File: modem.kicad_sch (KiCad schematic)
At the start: 14 parts, among them J1 A-1JB, J2 A-1JB, U1 BG95MxLA

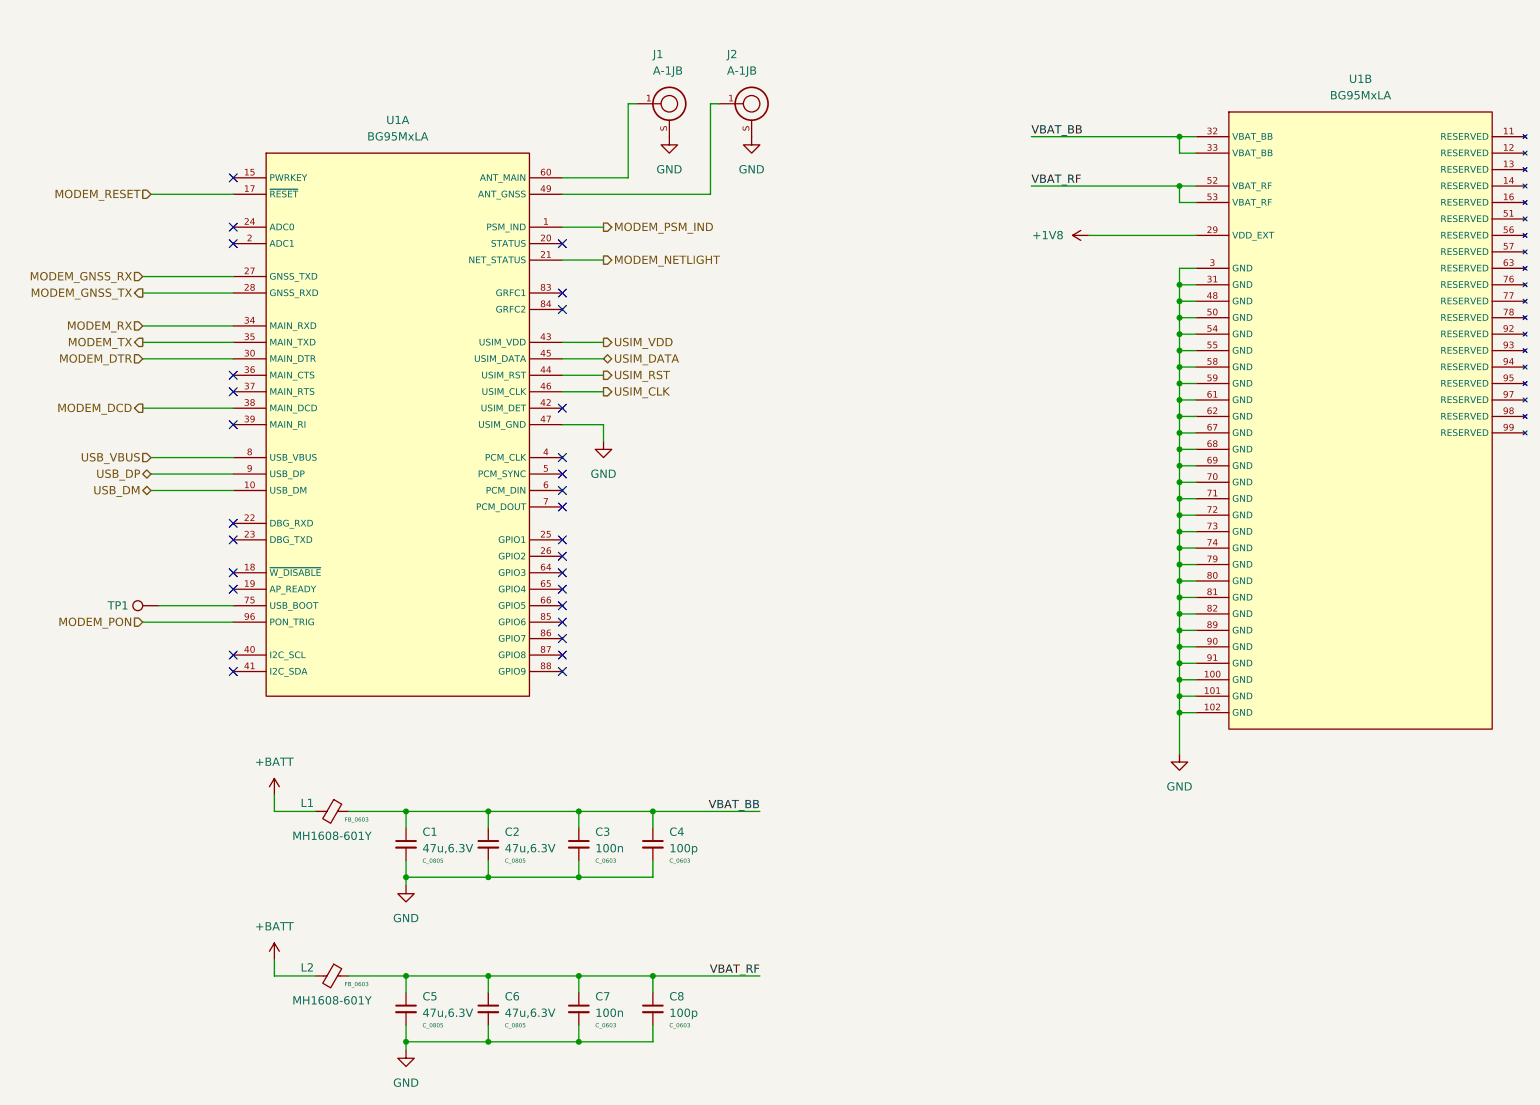
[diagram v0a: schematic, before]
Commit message: Remove PON_TRIG key, add PWRKEY control.
Remove USIM options on PCIE interface.
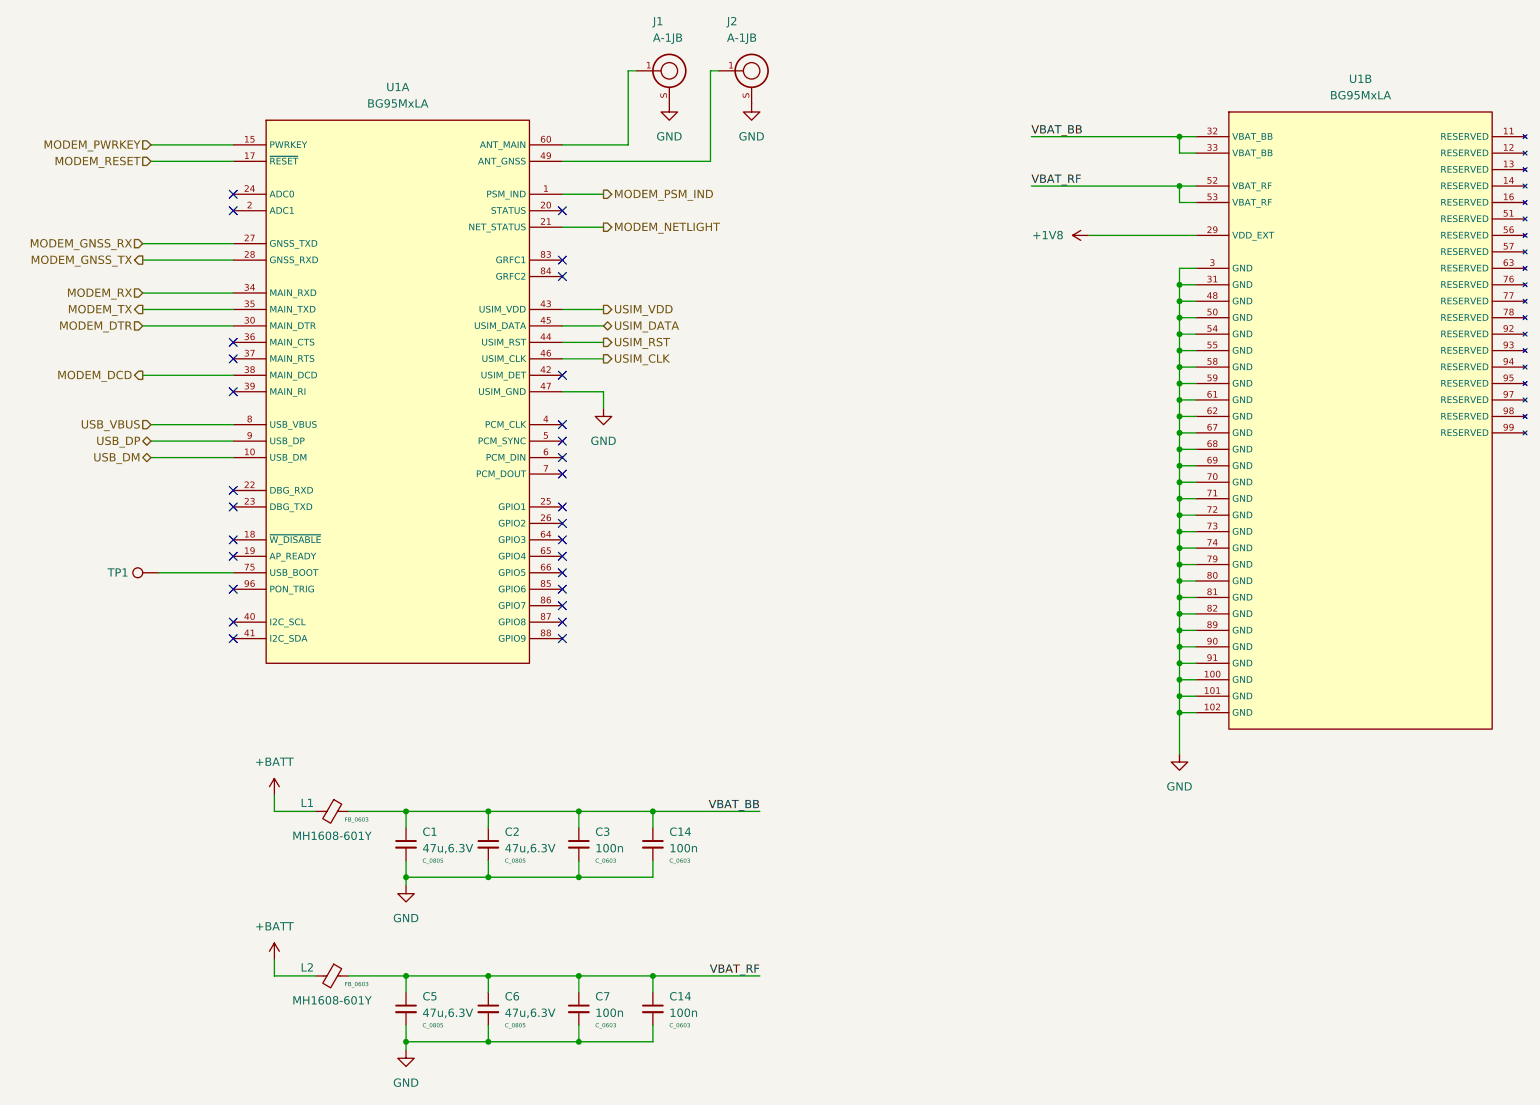
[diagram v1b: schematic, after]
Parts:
- removed C4, C8: 100p, C_Capacitor:C_0603, symbol C_Capacitor:C_0603
- added C14 (x2): 100n, C_Capacitor:C_0603, symbol C_Capacitor:C_0603
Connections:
- net GND: now also C14.2, C14.2
- net VBAT_BB: now also C14.1
- net VBAT_RF: now also C14.1
- net MODEM_PWRKEY: now reaches U1.15 (PWRKEY)
- net MODEM_PON: no longer names the net of U1.96 (PON_TRIG)
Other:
- moved on the sheet: J1, J2, TP1, U1A

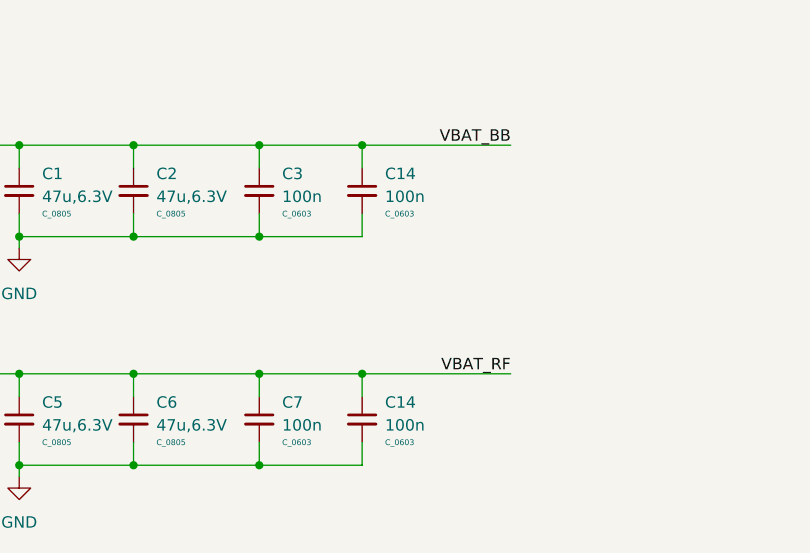
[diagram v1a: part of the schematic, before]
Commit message: Added tooling holes
Updated the readme
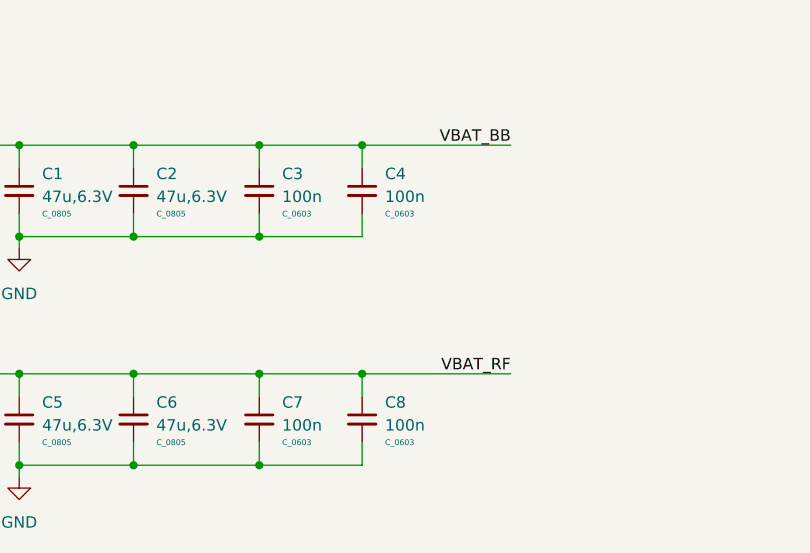
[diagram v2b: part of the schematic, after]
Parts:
- renumbered C14 to C4, C14 to C8

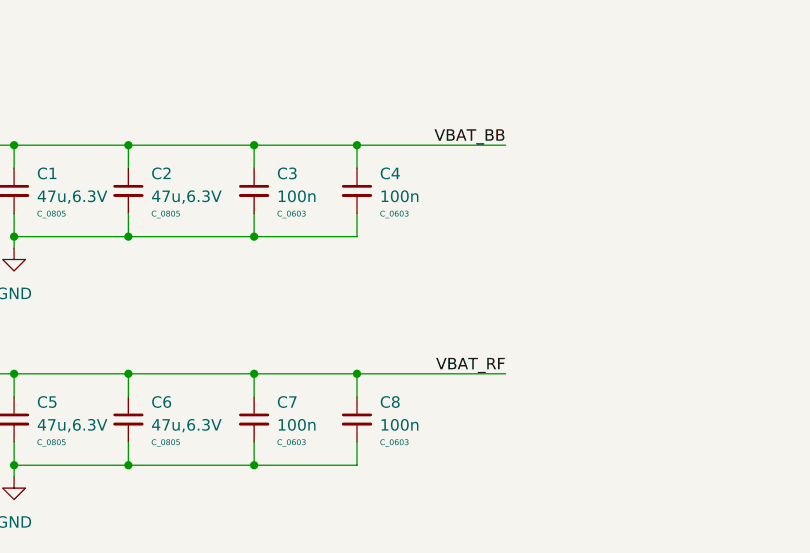
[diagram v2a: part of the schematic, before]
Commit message: Fix 33p caps
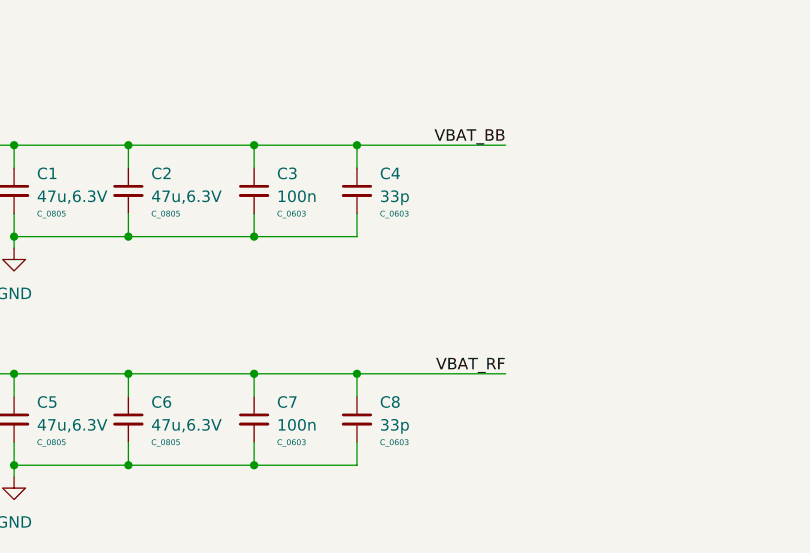
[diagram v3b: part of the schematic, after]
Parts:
- C4, C8: value 100n -> 33p
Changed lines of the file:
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@@
 		(fields_autoplaced yes)
 		(property "Reference" "C4"
-			(at 125.73 147.9613 0)
-			(effects
-				(font
-					(size 1.27 1.27)
-				)
-				(justify left)
-			)
-		)
-		(property "Value" "100n"
-			(at 125.73 150.5013 0)
+			(at 125.73 147.9612 0)
+			(effects
+				(font
+					(size 1.27 1.27)
+				)
+				(justify left)
+			)
+		)
+		(property "Value" "33p"
+			(at 125.73 150.5012 0)
 			(effects
 				(font
@@
 		(fields_autoplaced yes)
 		(property "Reference" "C8"
-			(at 125.73 173.3613 0)
-			(effects
-				(font
-					(size 1.27 1.27)
-				)
-				(justify left)
-			)
-		)
-		(property "Value" "100n"
-			(at 125.73 175.9013 0)
-			(effects
-				(font
+			(at 125.73 173.3612 0)
+			(effects
+				(font
+					(size 1.27 1.27)
+				)
+				(justify left)
+			)
+		)
+		(property "Value" "33p"
+			(at 125.73 175.9012 0)
+			(effects
+				(font

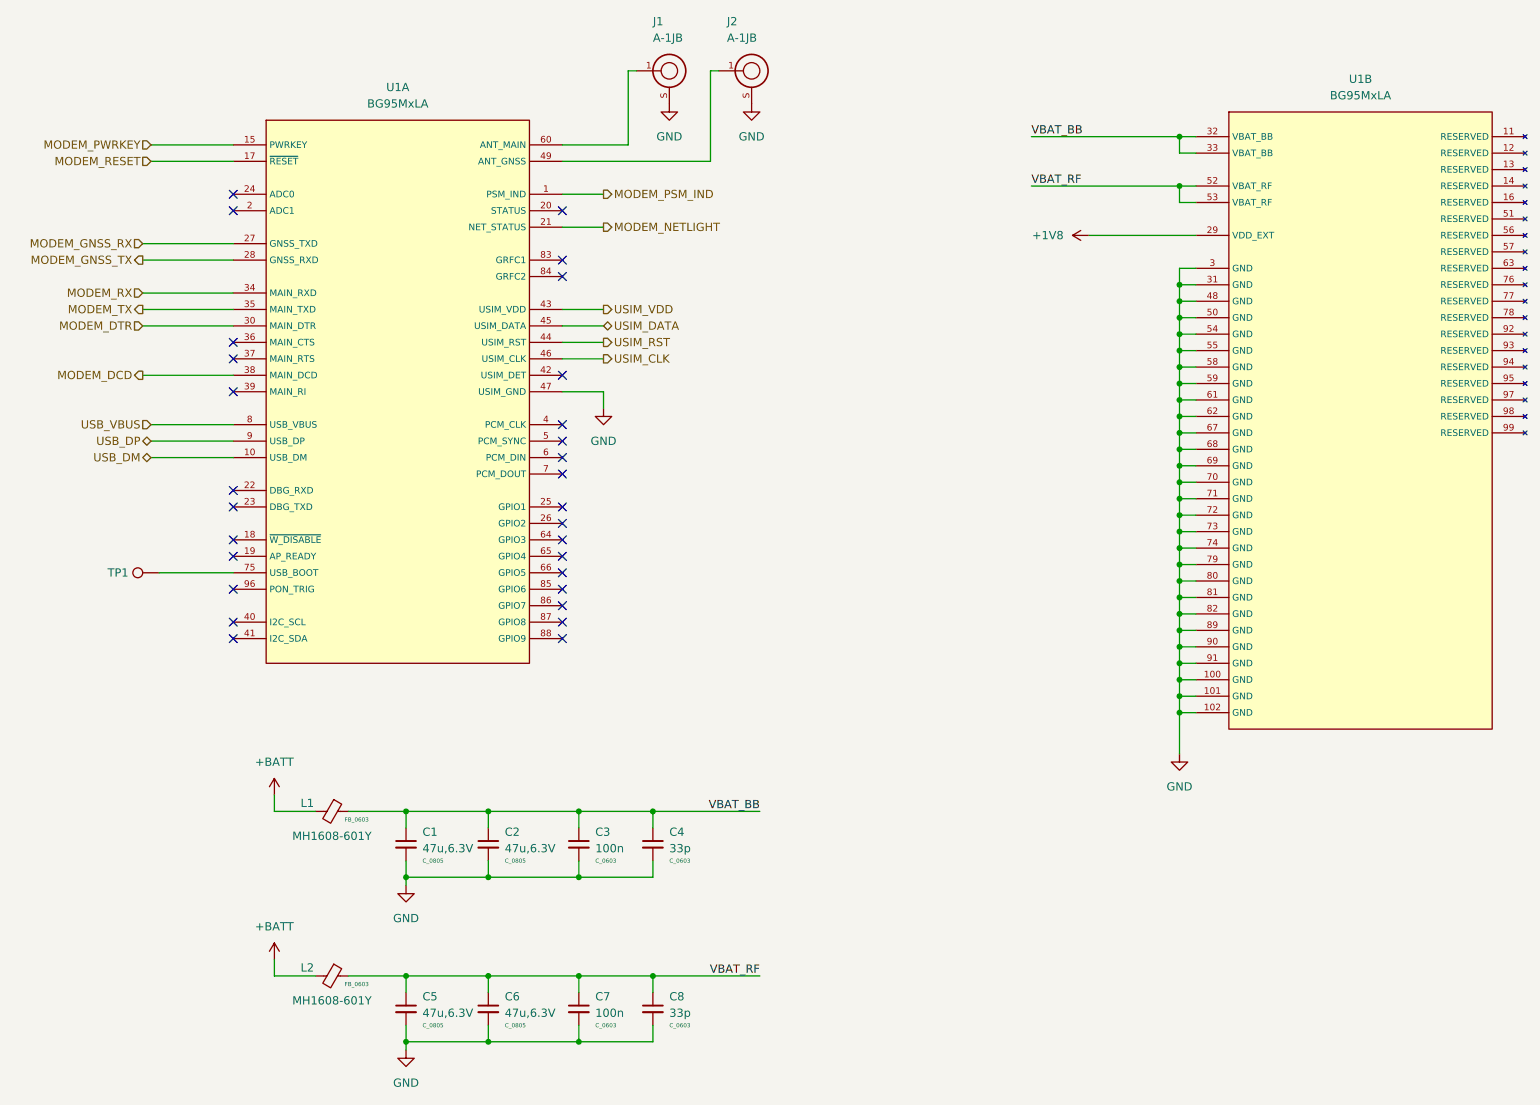
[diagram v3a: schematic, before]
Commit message: Implement fixes
Closes #2
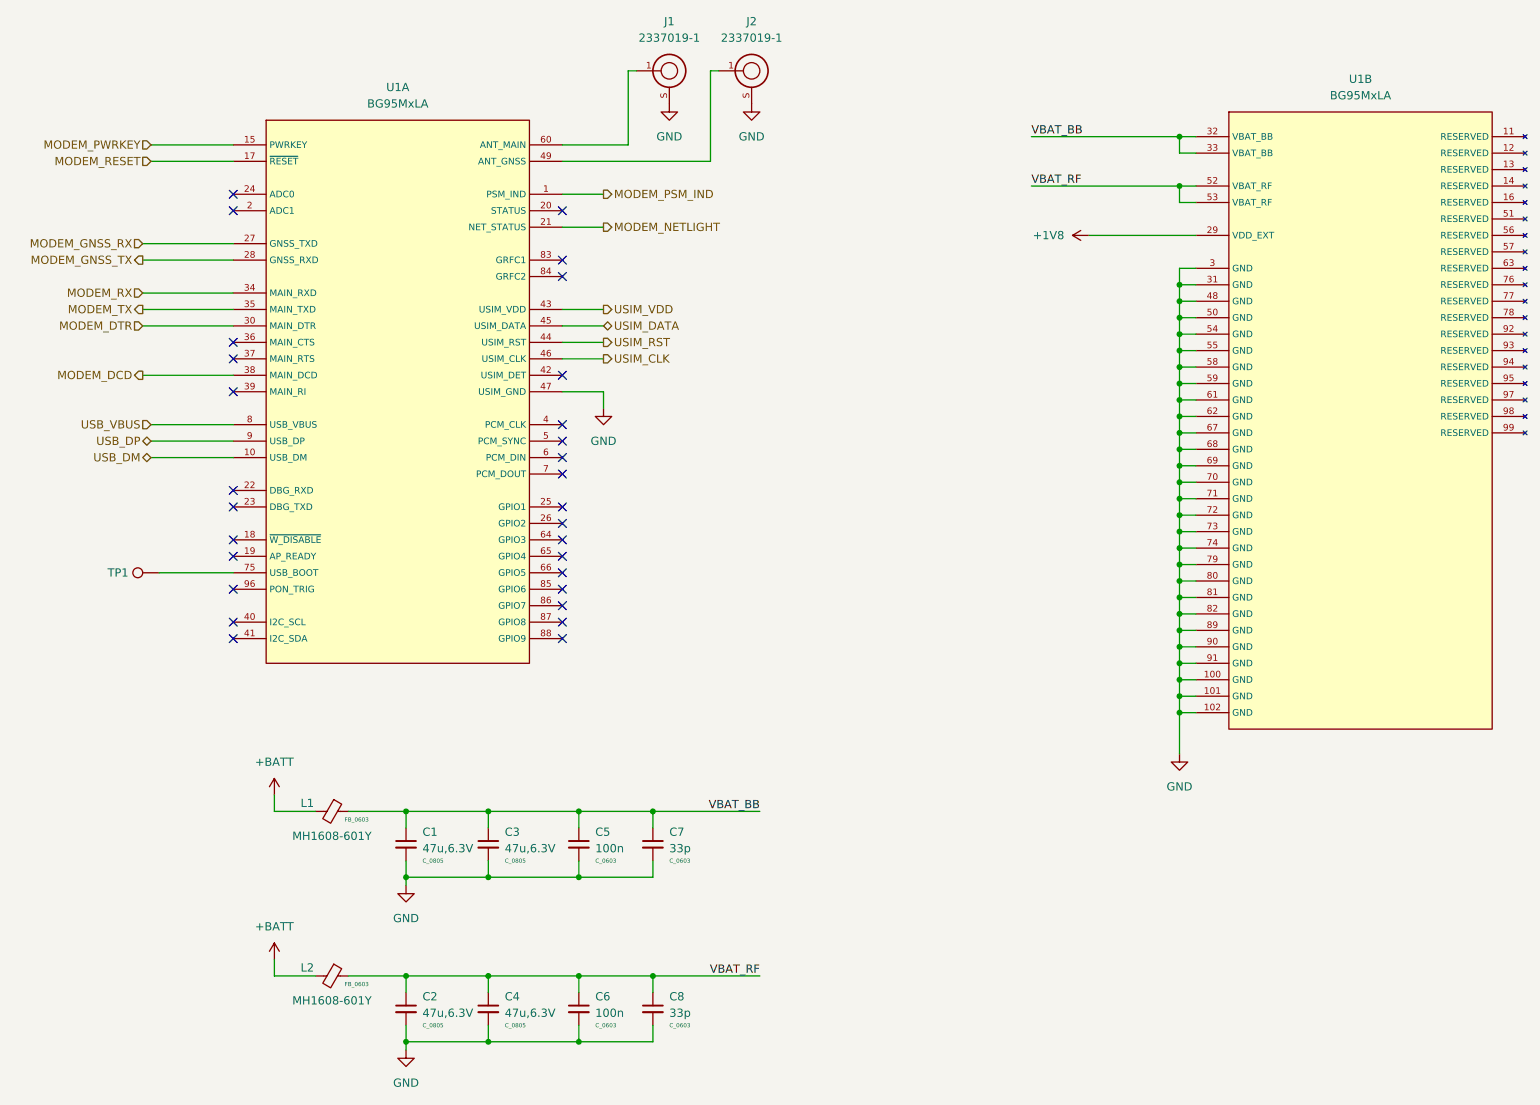
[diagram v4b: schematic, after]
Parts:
- removed J1, J2: A-1JB, J_Connector:A-1JB, symbol J_Connector:A-1JB
- removed TP1: ~, N_NonPart:TestPoint_1mm, symbol N_NonPart:TestPoint_1mm
- added J1, J2: 2337019-1, J_Connector:A-1JB, symbol J_Connector:2337019-1
- added TP1: ~, TP_TestPoint:TestPoint_1mm, symbol TP_TestPoint:TestPoint_1mm
- renumbered C5 to C2, C2 to C3, C6 to C4, C3 to C5, C7 to C6, C4 to C7
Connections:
- net GND: now also J1.S (SHIELD), J2.S (SHIELD)
- net at U1.75 (USB_BOOT): now also TP1.1
- net at U1.60 (ANT_MAIN): now also J1.1 (SIGNAL)
- net at U1.49 (ANT_GNSS): now also J2.1 (SIGNAL)
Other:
- company: (none) -> TL Embedded
- title: (none) -> Winglet BG95
